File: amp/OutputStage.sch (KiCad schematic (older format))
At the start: 25 parts

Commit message: started vac layout
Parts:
- removed SW?: SW_4PDT_x4, symbol synth:SW_4PDT_x4
- added C3, C4: 2.2u, KiCad/Capacitors_ThroughHole.pretty:CP_Radial_D6.3mm_P2.50mm, symbol Device:C
- added J11: EXT_IN, synth:3.5MM_Jack_Breakout_Vertical, symbol synth:AudioJack2_Ground_Switch
- added J12: A_OUT, synth:3.5MM_Jack_Breakout_Vertical, symbol synth:AudioJack2_Ground_Switch
- added J13: C_OUT, synth:3.5MM_Jack_Breakout_Vertical, symbol synth:AudioJack2_Ground_Switch
- added J14: B_OUT, synth:3.5MM_Jack_Breakout_Vertical, symbol synth:AudioJack2_Ground_Switch
- added J15: D_OUT, synth:3.5MM_Jack_Breakout_Vertical, symbol synth:AudioJack2_Ground_Switch
- added J17: HP_OUT, synth:3.5MM_Jack_Breakout_Vertical, symbol synth:AudioJack2_Ground_Switch
- added R10, R9: 200K, KiCad/Resistors_ThroughHole.pretty:R_Axial_DIN0204_L3.6mm_D1.6mm_P1.90mm_Vertical, symbol Device:R
- added R15, R16: 10K, KiCad/Resistors_ThroughHole.pretty:R_Axial_DIN0204_L3.6mm_D1.6mm_P1.90mm_Vertical, symbol Device:R
- added R17, R18, R19, R20: 470, KiCad/Resistors_ThroughHole.pretty:R_Axial_DIN0204_L3.6mm_D1.6mm_P1.90mm_Vertical, symbol Device:R
- added unit 4 of SW1
- added unit 4 of U2
- added unit 4 of U3
- C1, C2: renamed from C?; value 1u -> 2.2u
- J16: renamed from J?; footprint (none) -> KiCad/kicad-footprints/Connector_PinHeader_2.54mm.pretty:PinHeader_1x03_P2.54mm_Vertical
- R1, R11, R12, R2, R3, R4, R5, R6, R7, R8: renamed from R?; value 26K -> 200K
- R13, R14: renamed from R?; value R -> 10K
- RV1: renamed from RV?; footprint (none) -> KiCad/kicad-footprints/Connector_PinHeader_2.54mm.pretty:PinHeader_2x03_P2.54mm_Vertical
- SW1: renamed from SW?; footprint (none) -> KiCad/kicad-footprints/Connector_PinHeader_2.54mm.pretty:PinHeader_2x06_P2.54mm_Vertical
- SW1: renamed from SW?; value SW_4PDT_x4 -> SW_STEREO_SPLIT; footprint (none) -> KiCad/kicad-footprints/Connector_PinHeader_2.54mm.pretty:PinHeader_2x06_P2.54mm_Vertical
- U4: renamed from U?; footprint (none) -> KiCad/kicad-footprints/Package_DIP.pretty:DIP-8_W7.62mm
- gave numbers to parts that had none: 2
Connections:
- net -12VA: now also R15.2, R16.2
- net A_OUT: now also J12.T; no longer R1.2, R2.2
- net B_OUT: now also J14.T; no longer R3.2, R4.2
- net C_OUT: now also J13.T; no longer R5.2, R6.2
- net D_OUT: now also J15.T; no longer R7.2, R8.2
- net GND: now also J11.G, J11.S, J11.SN, J11.TN, J12.G, J12.S, J12.SN, J13.G, J13.S, J13.SN, J14.G, J14.S, J14.SN, J15.G, J15.S, J15.SN, J17.G
- net L_MIX: now also SW1.6 (C), SW1.7 (A), R10.1, SW1.12 (C); no longer SW1.12 (C), SW1.7 (A)
- net R_MIX: now also SW1.4 (A), SW1.9 (C), R9.1, SW1.10 (A); no longer SW1.10 (A), SW1.9 (C)
- net at RV1.2, U2.10: now also U2.7
- net at C2.2, R14.1: now also U3.9; no longer U3.8
- net at RV1.5: now also U3.10, U3.7; no longer U3.7
- net at R4.1: now also SW1.5 (B)
- net at R6.1: now also SW1.8 (B); no longer SW1.8 (B)
- net at R8.1: now also SW1.11 (B); no longer SW1.11 (B)
- net LEFT_OUT: no longer names the net of C1.1
- net LEFT_OUT: now also R17.2; no longer J16.T
- net RIGHT_OUT: no longer names the net of C2.1
- net RIGHT_OUT: now also R18.2; no longer J16.R
- new net: C4.2, R16.1, U2.8
- new net: C4.1, R20.2
- new net: C3.2, R15.1, U3.8
- new net: C3.1, R19.2
- new net: J11.T, R10.2, R9.2
- new net A_OUT_MIX: J12.TN, R1.2, R2.2
- new net B_OUT_MIX: J14.TN, R3.2, R4.2
- new net C_OUT_MIX: J13.TN, R5.2, R6.2
- new net D_OUT_MIX: J15.TN, R7.2, R8.2
- new net HP_LEFT_OUT: J17.T, R20.1
- new net HP_RIGHT_OUT: J17.S, R19.1
- new net MAIN_LEFT_OUT: J16.T, R17.1
- new net MAIN_RIGHT_OUT: J16.R, R18.1
- no-connect marks 0 -> 2
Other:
- note added: "Allow an external signal to get added here\n(e.g. output from another synth)"
- note added: "Each signal goes through 2x 200K res to a virtual ground, effectively\nsetting R1=100K. Rf=200K for a gain=2"
- note removed: "For VCA to clip above CV=5V, we need to amplify the output current to a\nvoltage close to the clipping of the op-amp. A gain of 2 puts the output\nclose to the rails, so an overdrive ought to risk clipping"
- note removed: "TODO: I don’t think compensating for the error in these resistors\nis super necessary, but hand-matching resistors or buying 1% or 5%\nmight be a smart move."
- note removed: "TODO: we’ve got 2 more buffers, should we add\na separate headphone out?"
- moved on the sheet: C1, J16, R13, U2B

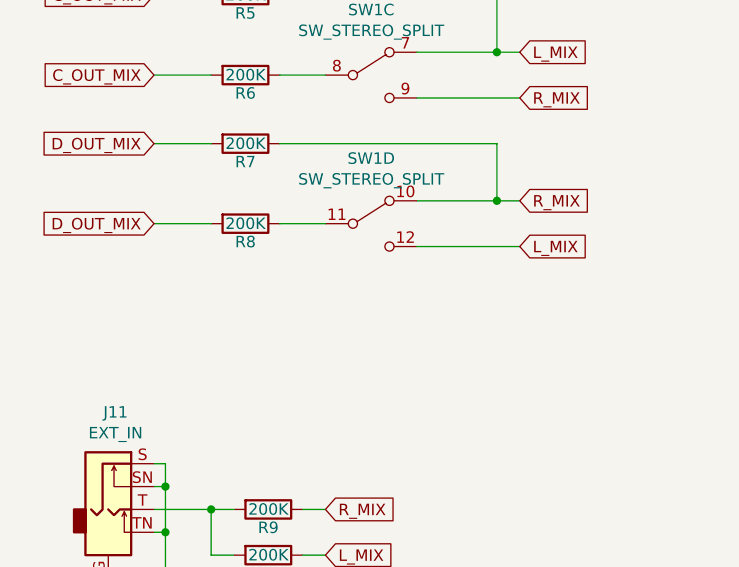
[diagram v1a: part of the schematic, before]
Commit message: update components
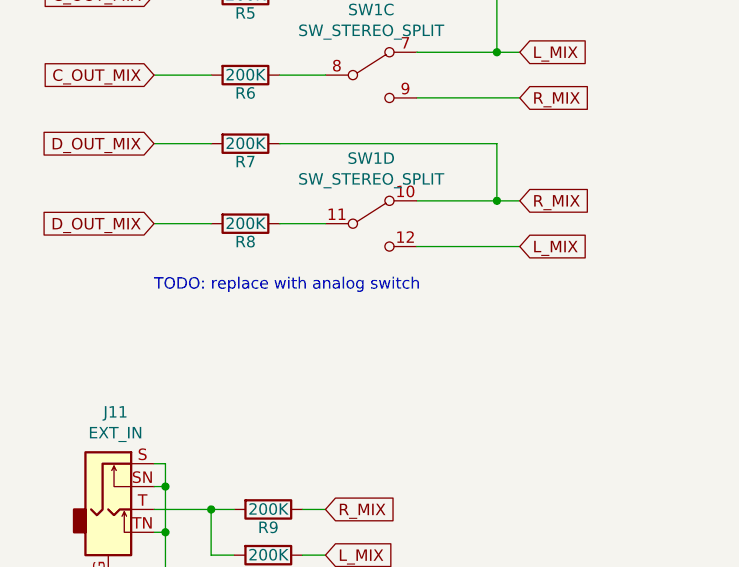
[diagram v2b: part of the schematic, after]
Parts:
- C1, C2, C3, C4: footprint KiCad/Capacitors_ThroughHole.pretty:CP_Radial_D6.3mm_P2.50mm -> Capacitor_THT:C_Radial_D6.3mm_H5.0mm_P2.50mm
- J16: footprint KiCad/kicad-footprints/Connector_PinHeader_2.54mm.pretty:PinHeader_1x03_P2.54mm_Vertical -> Connector_PinHeader_2.54mm:PinHeader_1x03_P2.54mm_Vertical
- R1, R10, R11, R12, R13, R14, R15, R16, R17, R18, R19, R2, R20, R3, R4, R5, R6, R7, R8, R9: footprint KiCad/Resistors_ThroughHole.pretty:R_Axial_DIN0204_L3.6mm_D1.6mm_P1.90mm_Vertical -> Resistor_THT:R_Axial_DIN0204_L3.6mm_D1.6mm_P1.90mm_Vertical
- RV1: footprint KiCad/kicad-footprints/Connector_PinHeader_2.54mm.pretty:PinHeader_2x03_P2.54mm_Vertical -> Connector_PinHeader_2.54mm:PinHeader_2x03_P2.54mm_Vertical
- SW1: footprint KiCad/kicad-footprints/Connector_PinHeader_2.54mm.pretty:PinHeader_2x06_P2.54mm_Vertical -> Connector_PinHeader_2.54mm:PinHeader_2x06_P2.54mm_Vertical
- U2, U3: footprint KiCad/Housings_DIP.pretty:DIP-16_W7.62mm -> Package_DIP:DIP-16_W7.62mm
- U4: footprint KiCad/kicad-footprints/Package_DIP.pretty:DIP-8_W7.62mm -> Package_DIP:DIP-8_W7.62mm
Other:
- note added: "TODO: replace with analog switch"
